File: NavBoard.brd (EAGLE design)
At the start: 91.1 x 50.8 mm, 15 parts, among them J1 APP_2POS_CONFIG12V_HORIZ, U2 LSM9DS1, U3 OKI-78SR-5/1.5-W36HC

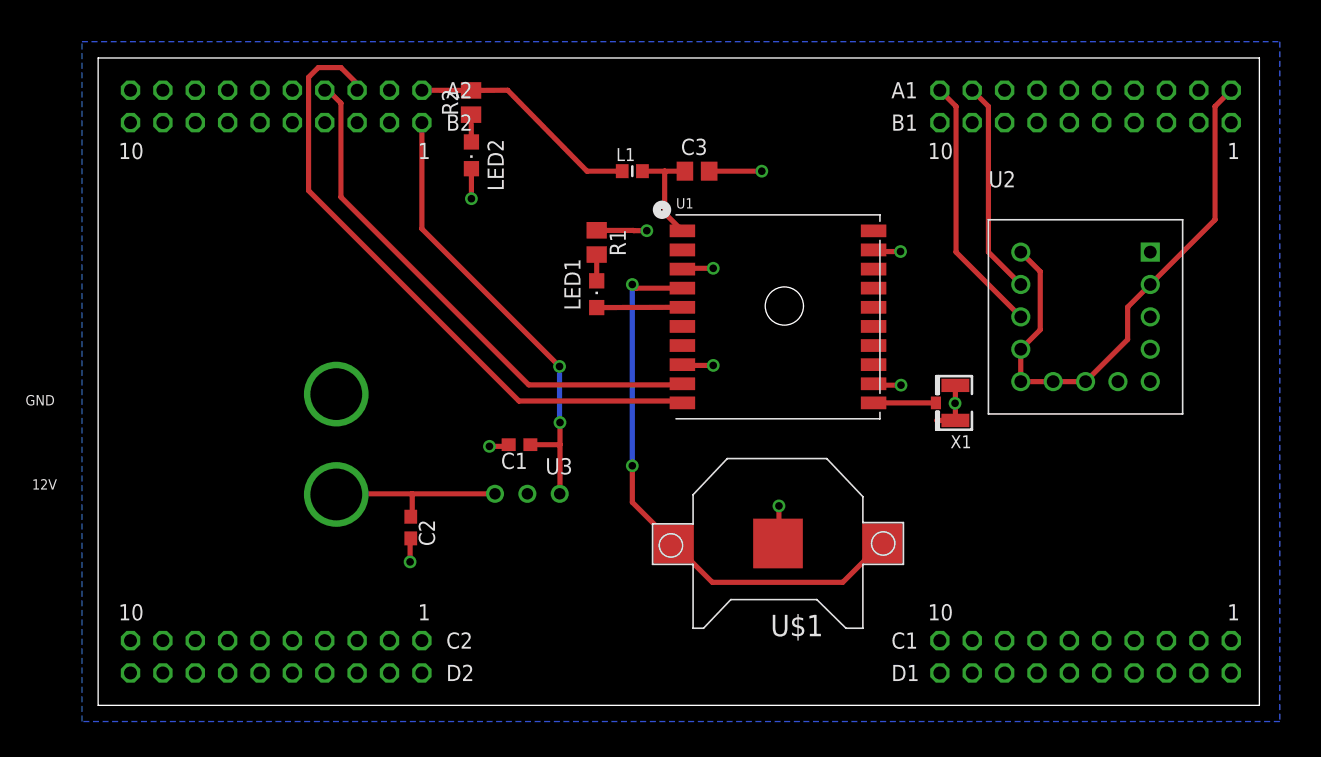
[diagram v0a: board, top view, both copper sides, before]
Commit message: Finished revision 1 of board design
Schematic: Connected INTM, INT1, INT2, and DRDYM from IMU to pins PL0
through PL3 on the Tiva. Added two new capacitors to power input of the
GPS chip. Added a capacitor to the battery power supply.
Board: Added top layer ground plane with ground plane stitching, added
mounting holes for the navigation board, arranged all component names on
board so they would be visible once they were silk screened, and added
text block with school name, team, logo, and board name.
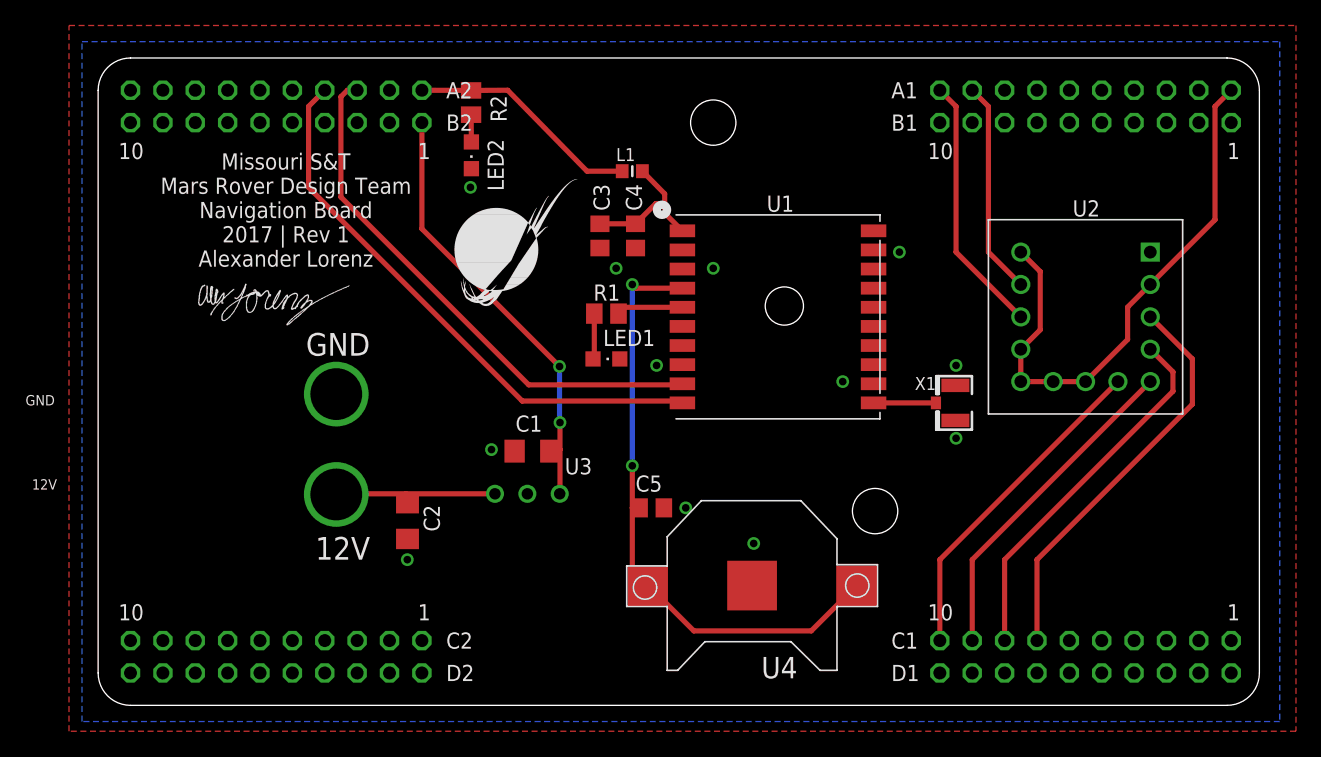
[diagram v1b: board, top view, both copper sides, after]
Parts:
- added C4: 0.01uF, resistor:C0805
- added C5: 1uF, resistor:C0805
- added LOGO1: MRDT_LOGO, MRDT-Hardware:MRDT_LOGO
- added U$3, U$4: (no value), MRDT-Hardware:#6_SCREW
- added U4: (no value), adafruit:CR1220-SMD
- C1, C2: device resistor:C0603 -> resistor:C1206
- C3: value 0.1 uF -> 1uF; device rcl:C0805 -> resistor:C0805
- U$1: device adafruit:CR1220-SMD -> sig:SIG
- moved U$1 48.8 mm to (7.37, 29.0), turned to 0 degrees
- moved C3 9.16 mm to (39.4, 36.8), turned to 270 degrees
- moved R1 5.64 mm to (39.9, 30.7), turned to 0 degrees
- moved LED1 5.14 mm to (39.9, 27.2), turned to 270 degrees
- moved C1 1.14 mm to (34.1, 19.9)
- moved C2 0.57 mm to (24.3, 14.5)
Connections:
- removed net N$23: LED1.C, R1.2
- removed net N$6: LED1.A, U1.P$5
- new net DRDYM: U$2.PL3, U2.6
- new net INT1: U$2.PL1, U2.4
- new net INT2: U$2.PL0, U2.3
- new net INTM: U$2.PL2, U2.5
- new net N$2: LED1.A, R1.1
- new net N$3: R1.2, U1.P$5
- net GND: now also C4.2, C5.2, LED1.C, U4.-; no longer R1.1, U$1.-
- net N$24: now also C4.1
- net RX(6): now also U$2.PP1; no longer U$2.PP0
- net TX(6): now also U$2.PP0; no longer U$2.PP1
- net VBACKUP: now also C5.1, U4.+$1, U4.+$2; no longer U$1.+$1, U$1.+$2
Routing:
- net INT2: track 0.00 -> 31.8 mm
- net GND: track 30.5 -> 0.00 mm, vias 11 -> 12
- net INT1: track 0.00 -> 29.1 mm
- net INTM: track 0.00 -> 26.1 mm
- net DRDYM: track 0.00 -> 26.1 mm
- net N$6: track 6.72 -> 0.00 mm
- net RX(6): track 50.3 -> 44.5 mm
- net N$3: track 0.00 -> 5.22 mm
- net N$2: track 0.00 -> 3.60 mm
- net N$24: track 8.59 -> 11.7 mm
- net VBACKUP: track 44.6 -> 47.6 mm
- net N$23: track 2.06 -> 0.00 mm
- net TX(6): track 42.0 -> 43.6 mm
- net +5V: track 36.0 -> 34.4 mm
- net N$1: track 14.3 -> 13.2 mm
- added copper zone on layer 1, net GND
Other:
- outline, holes or cut-outs redrawn
- board text added: "12V"
- board text added: "GND"
- board text added: "Missouri S&T Mars Rover Design Team Navigation Board 2017 | Rev 1 Alexander Lorenz"
